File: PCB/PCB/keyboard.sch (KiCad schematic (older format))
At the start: 223 parts, among them SW1 SW_PUSH, SW2 SW_PUSH, U1 STM32F072CBUx, U2 MCP1700-3302E_SOT23

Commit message: V2 CAD finished.
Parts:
- removed D_90: D, Diode_SMD:D_SOD-123, symbol Device:D_Small
- K_0, K_1, K_10, K_100, K_11, K_12, K_13, K_14, K_15, K_16, K_17, K_18, K_19, K_2, K_20, K_21, K_22, K_23, K_24, K_25, K_26, K_27, K_28, K_29, K_3, K_30, K_32, K_33, K_34, K_35, K_37, K_38, K_39, K_4, K_40, K_41, K_42, K_43, K_44, K_45, K_46, K_47, K_48, K_5, K_50, K_51, K_52, K_55, K_56, K_57, K_58, K_59, K_6, K_60, K_61, K_62, K_63, K_64, K_65, K_67, K_68, K_69, K_7, K_71, K_72, K_73, K_74, K_75, K_76, K_77, K_78, K_79, K_8, K_80, K_82, K_83, K_84, K_85, K_9, K_96, K_97, K_98, K_99: footprint MX_Alps_Hybrid:MX-1U-NoLED -> MX_Only:MXOnly-1U-NoLED
- K_31: footprint MX_Alps_Hybrid:MX-2U-NoLED -> MX_Only:MXOnly-2U-NoLED
- K_36, K_49: footprint MX_Alps_Hybrid:MX-1.5U-NoLED -> MX_Only:MXOnly-1.5U-NoLED
- K_53, K_86: footprint MX_Alps_Hybrid:MX-1U-NoLED -> MX_Only:MXOnly-2U-NoLED
- K_54, K_81: footprint MX_Alps_Hybrid:MX-1.75U-NoLED -> MX_Only:MXOnly-1.75U-NoLED
- K_66, K_70, K_91: footprint MX_Alps_Hybrid:MX-2.25U-NoLED -> MX_Only:MXOnly-2.25U-NoLED
- K_87, K_88, K_89, K_92, K_94, K_95: footprint MX_Alps_Hybrid:MX-1.25U-NoLED -> MX_Only:MXOnly-1.25U-NoLED
- K_90: footprint MX_Alps_Hybrid:MX-6.25U-NoLED -> MX_Only:MXOnly-6.25U-NoLED
- K_93: footprint MX_Alps_Hybrid:MX-2.753U-NoLED -> MX_Only:MXOnly-2.75U-NoLED
- renumbered C7 to C1, C1 to C2, C2 to C7
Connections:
- net +3V3: no longer U1.1 (VBAT)
- net col0: now also U1.13 (PA3)
- net col1: now also U1.14 (PA4)
- net col10: now also U1.37 (PA14)
- net col11: now also U1.38 (PA15)
- net col12: now also U1.39 (PB3)
- net col13: now also U1.40 (PB4)
- net col14: now also U1.41 (PB5)
- net col15: now also U1.42 (PB6)
- net col16: now also U1.43 (PB7)
- net col17: now also U1.45 (PB8)
- net col18: now also U1.46 (PB9)
- net col2: now also U1.15 (PA5)
- net col3: now also U1.16 (PA6)
- net col4: now also U1.17 (PA7)
- net col5: now also U1.18 (PB0)
- net col6: now also U1.19 (PB1)
- net col7: now also U1.20 (PB2)
- net col8: now also U1.21 (PB10)
- net col9: now also U1.22 (PB11)
- net row0: now also U1.10 (PA0)
- net row1: now also U1.6 (PF1)
- net row2: now also U1.5 (PF0)
- net row3: now also U1.4 (PC15)
- net row4: now also U1.3 (PC14)
- net row5: now also U1.2 (PC13)
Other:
- moved on the sheet: K_90

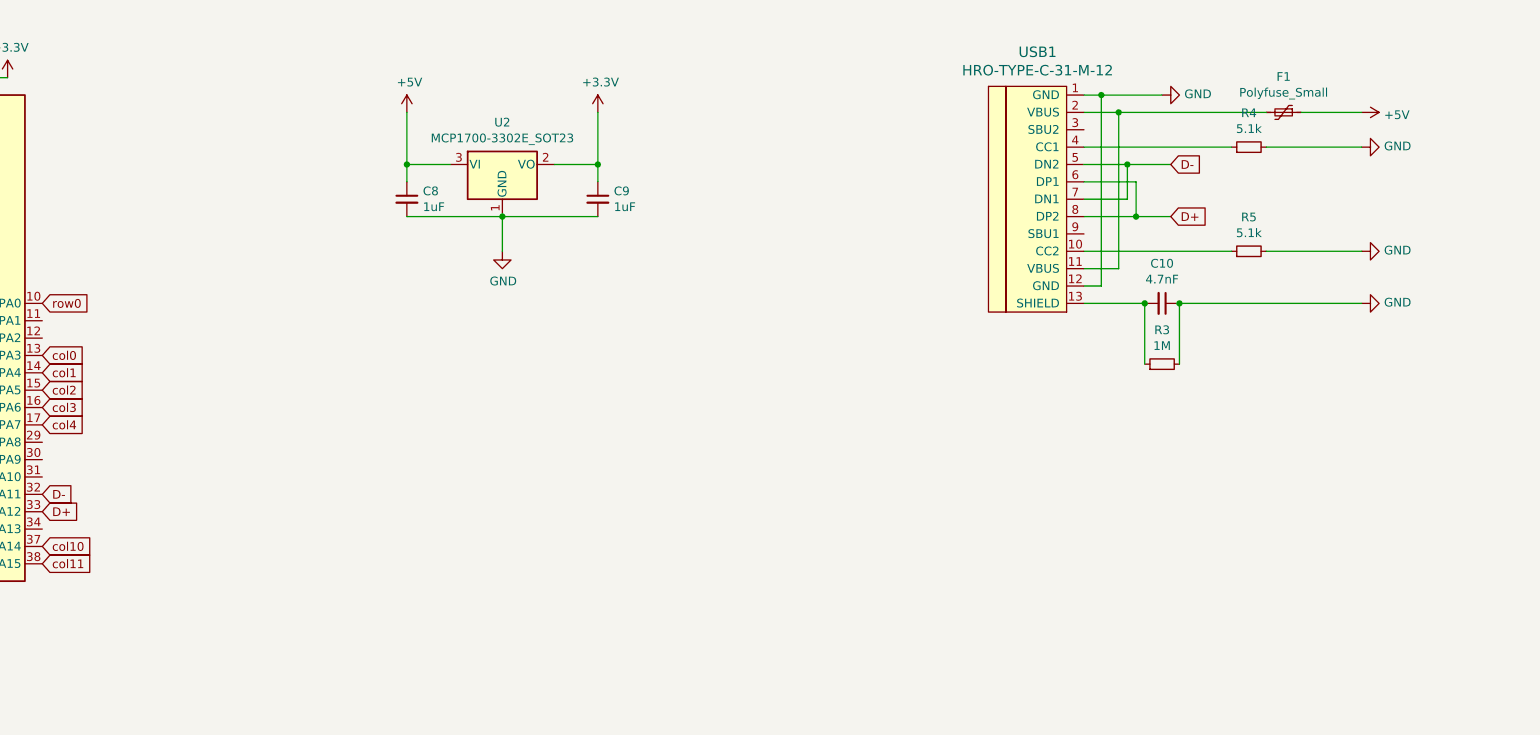
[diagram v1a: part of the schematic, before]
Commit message: Added ESD Protection to PCB
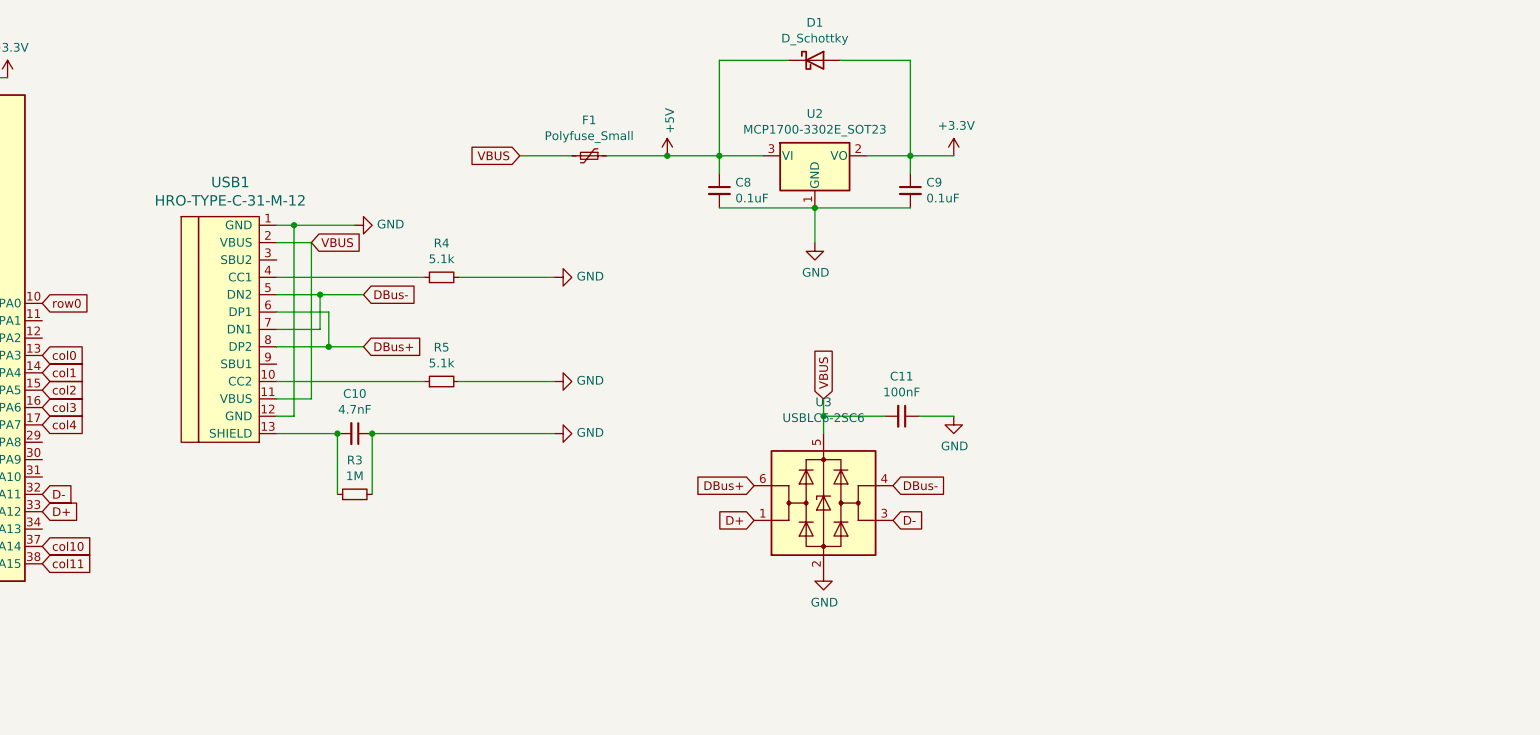
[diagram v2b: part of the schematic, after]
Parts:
- added C11: 100nF, Capacitor_SMD:C_0603_1608Metric, symbol Device:C_Small
- added D1: D_Schottky, Diode_SMD:D_SOD-123, symbol Device:D_Schottky
- added U3: USBLC6-2SC6, Package_TO_SOT_SMD:SOT-23-6, symbol Power_Protection:USBLC6-2SC6
- C8, C9: value 1uF -> 0.1uF
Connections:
- net +3V3: now also D1.2 (A)
- net +5V: now also D1.1 (K)
- net D+: now also U3.1 (I/O1); no longer USB1.6 (DP1), USB1.8 (DP2)
- net D-: now also U3.3 (I/O2); no longer USB1.5 (DN2), USB1.7 (DN1)
- net GND: now also C11.1, U3.2 (GND)
- net VBUS: now reaches F1.2, USB1.11 (VBUS), USB1.2 (VBUS)
- net VBUS: now also C11.2, U3.5 (VBUS)
- new net DBus+: U3.6 (I/O1), USB1.6 (DP1), USB1.8 (DP2)
- new net DBus-: U3.4 (I/O2), USB1.5 (DN2), USB1.7 (DN1)
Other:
- moved on the sheet: C10, C8, C9, F1, R3, R4, R5, U2, USB1
